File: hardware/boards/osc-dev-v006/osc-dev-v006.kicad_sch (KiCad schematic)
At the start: 4 parts

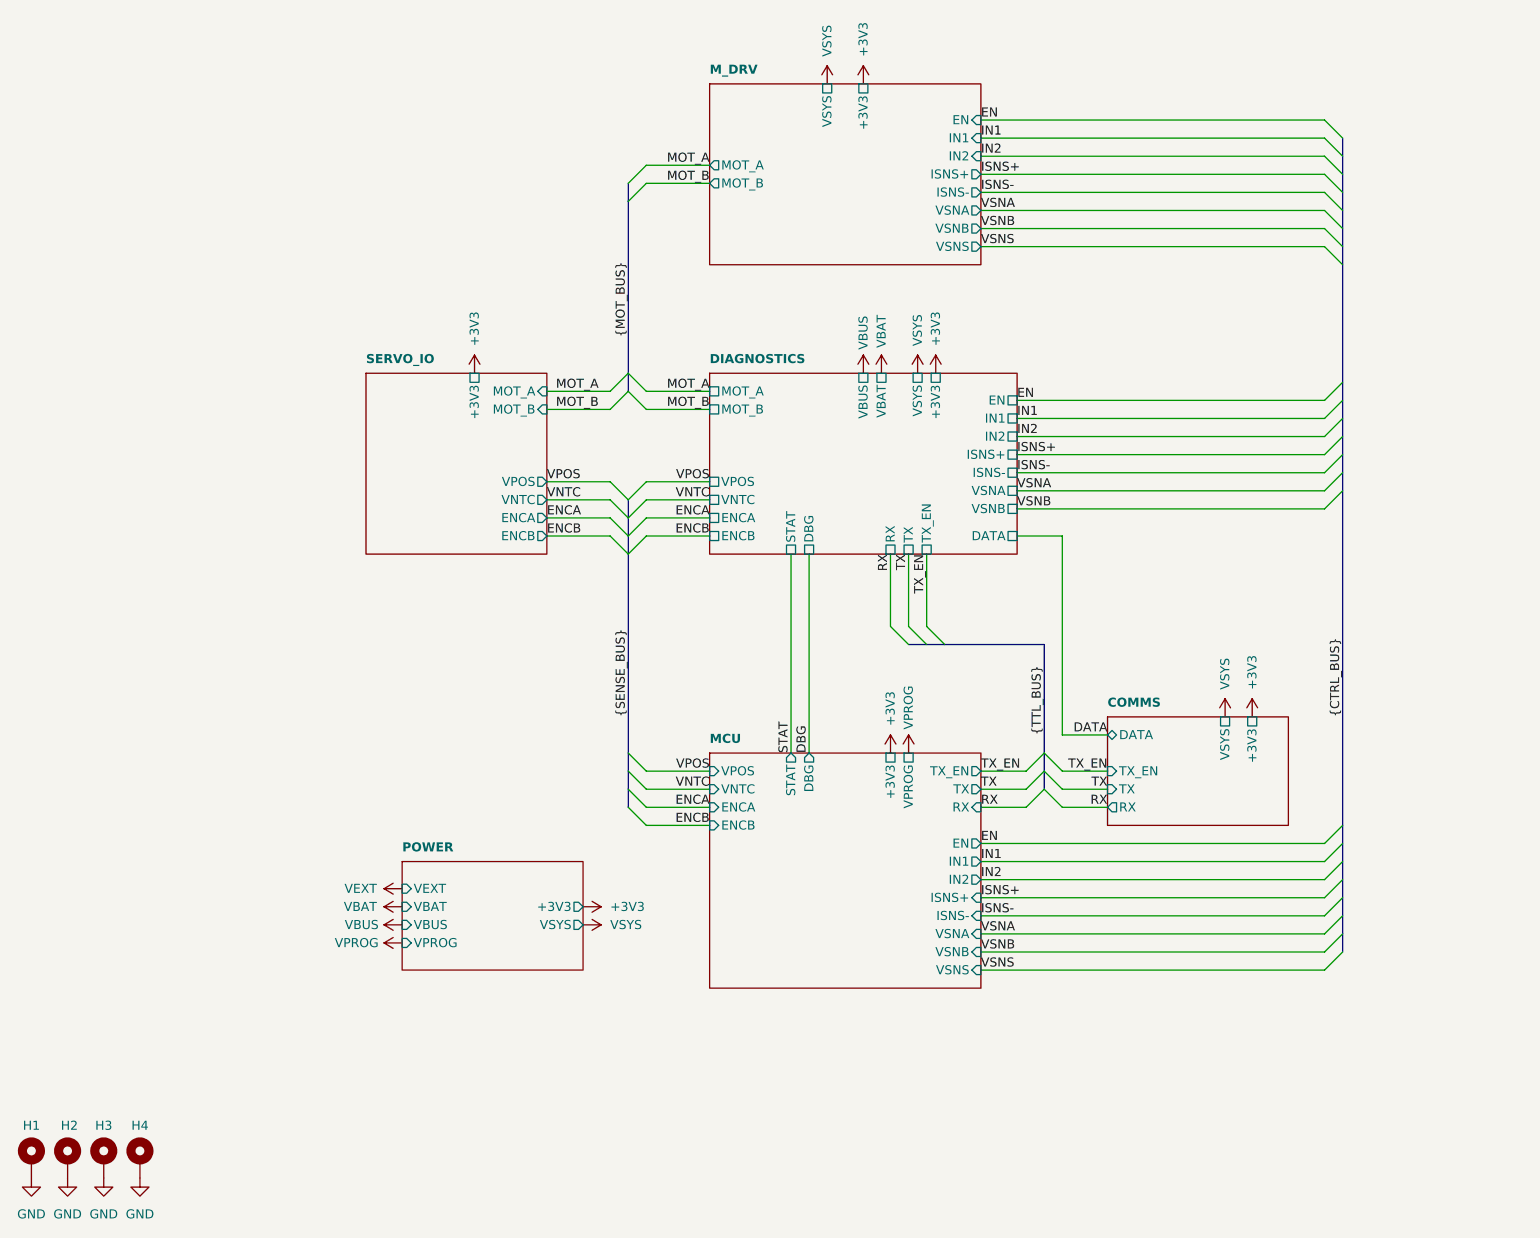
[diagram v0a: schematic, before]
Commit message: hw: osc-dev-v006 rev-2a - 6l precision respin, direct-wire bus, docs
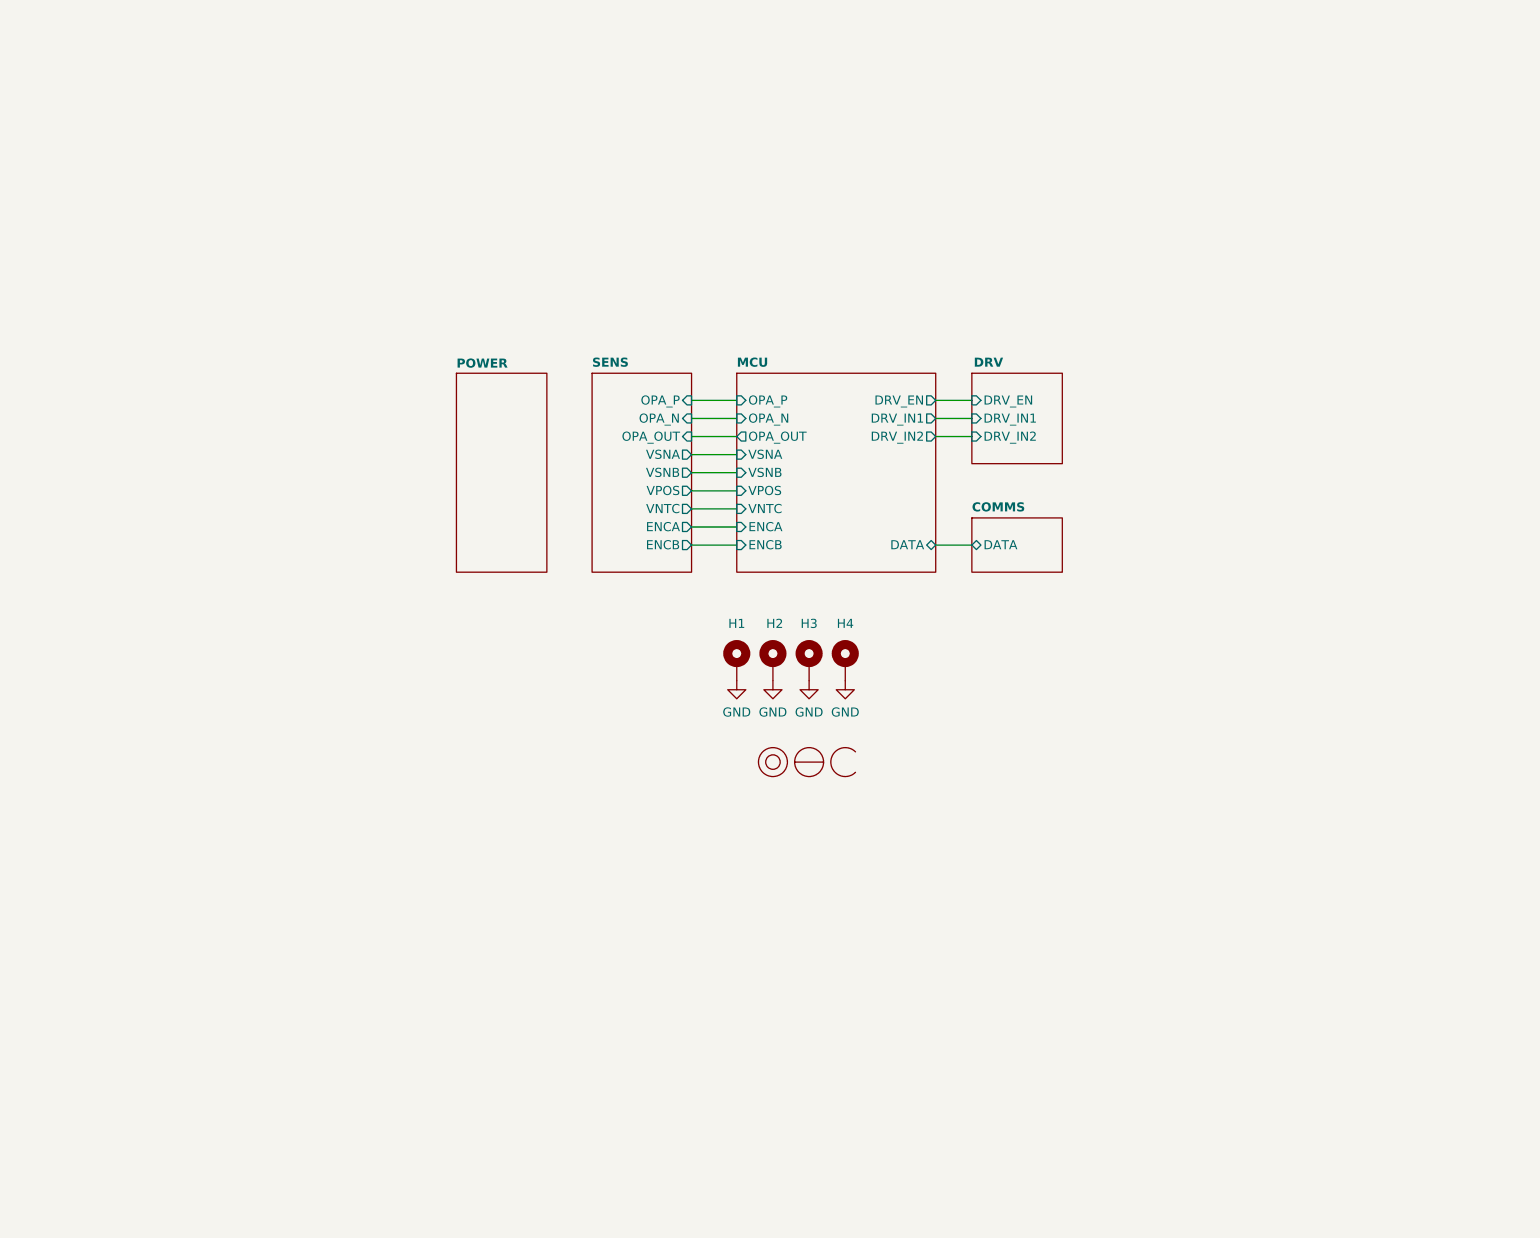
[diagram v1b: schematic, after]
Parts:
- added LOGO1: osc-logo, shared:osc, symbol shared:osc-logo
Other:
- sheet M_DRV renamed DRV
- removed sheet DIAGNOSTICS
- removed sheet SERVO_IO
- added sheet SENS (SENSORS.kicad_sch)
- sheet COMMS ports: added none; removed +3V3, RX, TX, TX_EN, VSYS
- sheet DRV ports: added DRV_EN, DRV_IN1, DRV_IN2; removed +3V3, EN, IN1, IN2, ISNS+, ISNS-, MOT_A, MOT_B, VSNA, VSNB, VSNS, VSYS
- sheet MCU ports: added DATA, DRV_EN, DRV_IN1, DRV_IN2, OPA_N, OPA_OUT, OPA_P; removed +3V3, DBG, EN, IN1, IN2, ISNS+, ISNS-, RX, STAT, TX, TX_EN, VPROG, VSNS
- sheet POWER ports: added none; removed +3V3, VBAT, VBUS, VEXT, VPROG, VSYS
- moved on the sheet: H1, H2, H3, H4

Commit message: board: osc-dev-v006 rev 2a (#107)
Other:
- sheet MCU ports: added VPOS1, VPOS2_NTC, VSNS; removed VNTC, VPOS
- sheet SENS ports: added VPOS1, VPOS2_NTC, VSNS; removed VNTC, VPOS
- moved on the sheet: H1, H2, H3, H4
